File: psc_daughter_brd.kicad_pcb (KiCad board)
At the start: 2 copper layers, 50 x 150 mm, 293 parts, among them J1 61082-061400LF, J2 61082-061400LF, U1 AD8221, U10 BUF634AxD, U11 BUF634AxD, U12 ADR1001AEZ, U13 ADS8568SPM, U14 AD8221, U15 OPA277, U16 AD8221, U17 OPA277, U18 AD8221, U19 OPA277, U2 OPA277, U26 LTC6655BHLS8-5, U27 AD8429BRZ, U28 AD8675ARZ, U29 LT6202CS5, U3 AD8676xR, U30 LTC6363xMS8, U31 LTC2376CDE-20-PBF, U32 LTC6655BHLS8-5, U33 AD8429BRZ, U34 AD8675ARZ, U35 LT6202CS5, U36 LTC6363xMS8, U37 LTC2376CDE-20-PBF, U38 TXUN0104RUTR, U39 ADUM5240ARZ, U4 AD8676xR, U40 ADUM5240ARZ, U41 TXUN0104RUTR, U42 ADUM5242ARZ, U43 ADUM5242ARZ, U5 AD5791BRUZ, U6 AD797, U7 OPA277, U8 OPA277, U9 OPA277

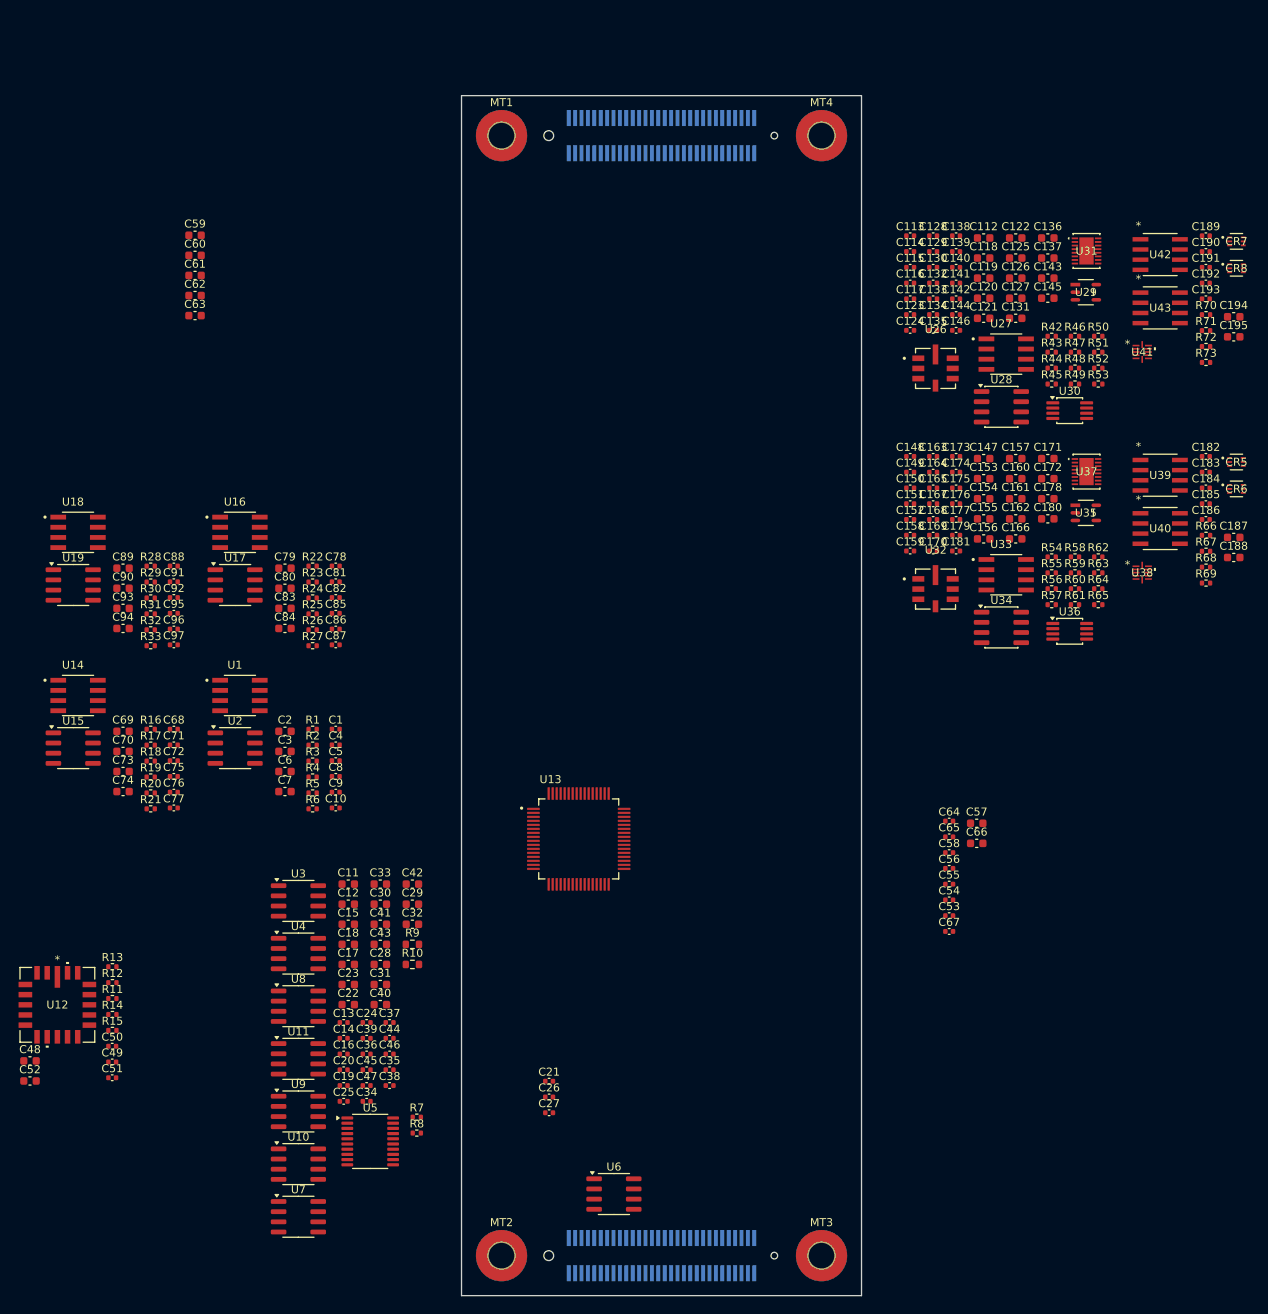
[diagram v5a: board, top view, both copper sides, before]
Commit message: DAC and DCCT placement
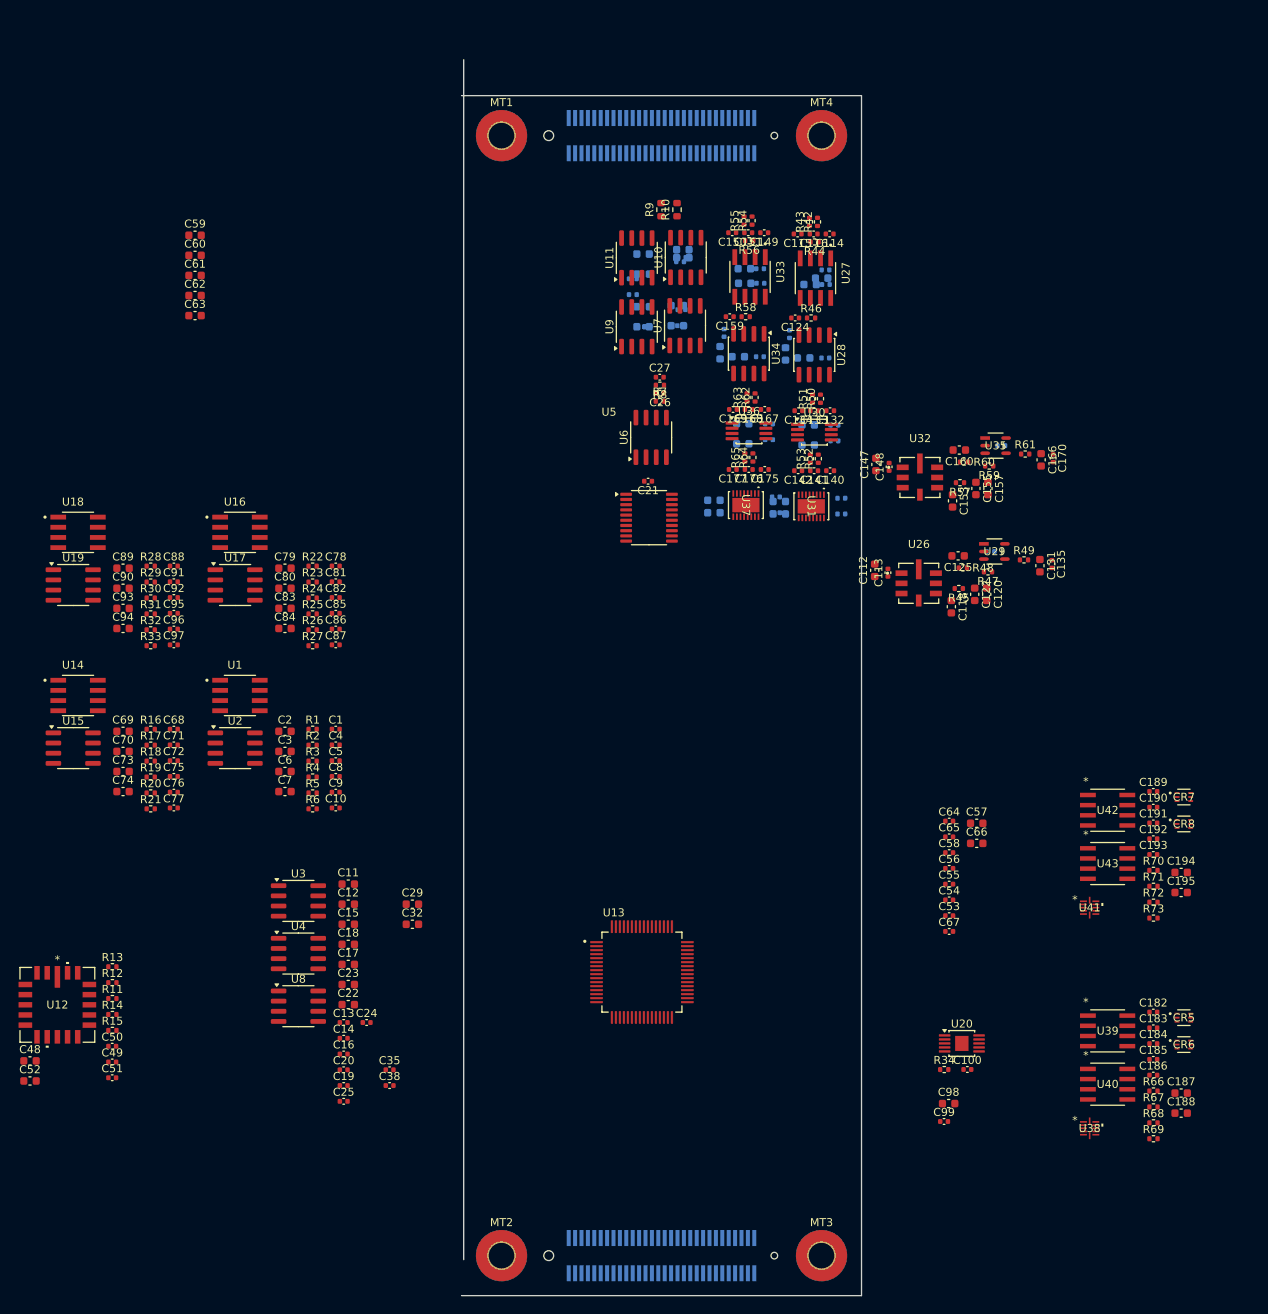
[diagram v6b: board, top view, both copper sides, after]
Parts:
- added C100: 0.47uF, Capacitor_SMD:C_0402_1005Metric, F.Cu at (202.9, 163.5)
- added C98: 10uF, Capacitor_SMD:C_0603_1608Metric, F.Cu at (200.6, 167.8)
- added C99: 0.1uF, Capacitor_SMD:C_0402_1005Metric, F.Cu at (200.0, 170.0)
- added R34: 121, Resistor_SMD:R_0402_1005Metric, F.Cu at (200.0, 163.5)
- added U20: LT3042xMSE, Package_SO:MSOP-10-1EP_3x3mm_P0.5mm_EP1.68x1.88mm, F.Cu at (202.2, 160.2)
- C117, C119, C121, C123, C126, C127, C128, C129, C130, C136, C137, C138, C139, C143, C144, C145, C146, C152, C154, C156, C158, C161, C162, C163, C164, C165, C171, C172, C173, C174, C178, C179, C180, C181, C28, C30, C31, C33, C34, C36, C37, C39, C40, C41, C42, C43, C44, C45, C46, C47: moved to B.Cu
- moved U10 123.2 mm to (167.7, 62.0), turned to 90 degrees
- moved U7 121.4 mm to (167.6, 70.5), turned to 90 degrees
- moved U11 108.7 mm to (161.6, 62.0), turned to 90 degrees
- moved U9 106.8 mm to (161.6, 70.7), turned to 90 degrees
- moved C46 105.5 mm to (167.0, 62.5), turned to 180 degrees
- moved C34 104.6 mm to (167.2, 70.5), turned to 180 degrees
- moved C45 104.3 mm to (161.1, 64.7), turned to 180 degrees
- moved C47 104.3 mm to (161.1, 66.6), turned to 180 degrees
- moved C44 104.2 mm to (167.3, 62.0), turned to 180 degrees
- moved C40 101.7 mm to (167.4, 61.0), turned to 180 degrees
- moved R10 100.0 mm to (166.6, 56.0), turned to 90 degrees
- moved R8 98.3 mm to (164.5, 78.0), turned to 180 degrees
- moved C36 97.1 mm to (162.1, 70.7), turned to 180 degrees
- moved R9 97.0 mm to (164.6, 56.0), turned to 90 degrees
- moved C37 96.3 mm to (167.2, 68.5), turned to 180 degrees
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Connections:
- net +10V renamed /DCCT ADCs/DCCT Channel 1/vref_in
- net /DCCT ADCs/dcct1_busy renamed /DCCT ADCs/DCCT Channel 2/busy
- C53 pad 1: Net-(C53-Pad1) -> +5.0V
- C54 pad 1: Net-(C53-Pad1) -> +5.0V
- C55 pad 1: Net-(C53-Pad1) -> +5.0V
- C56 pad 1: Net-(C53-Pad1) -> +5.0V
- C58 pad 1: Net-(C53-Pad1) -> +5.0V
- C65 pad 1: Net-(C53-Pad1) -> +5.0V
- J1 pad 1: unconnected-(J1-Pad1) -> /PS connector/dout_iso_gnd
- J1 pad 10: unconnected-(J1-Pad10) -> /PS connector/digin_acon
- J1 pad 11: unconnected-(J1-Pad11) -> /PS connector/din_iso_gnd
- J1 pad 12: /Isolated Digital IO/din0_iso -> /PS connector/digin_flt1
- J1 pad 13: unconnected-(J1-Pad13) -> /PS connector/din_iso_gnd
- J1 pad 14: /Isolated Digital IO/din1_iso -> /PS connector/digin_flt2
- J1 pad 15: unconnected-(J1-Pad15) -> /PS connector/din_iso_gnd
- J1 pad 16: /Isolated Digital IO/din2_iso -> /PS connector/digin_spare
- J1 pad 17: unconnected-(J1-Pad17) -> GND
- J1 pad 18: /Isolated Digital IO/din3_iso -> GND
- J1 pad 19: unconnected-(J1-Pad19) -> GND
- J1 pad 2: /Isolated Digital IO/dout0_iso -> /PS connector/digout_on1
- J1 pad 20: unconnected-(J1-Pad20) -> /Monitor ADCs/monitor_spare+
- J1 pad 21: unconnected-(J1-Pad21) -> GND
- J1 pad 22: unconnected-(J1-Pad22) -> /Monitor ADCs/monitor_spare-
- J1 pad 23: unconnected-(J1-Pad23) -> GND
- J1 pad 24: /Monitor ADCs/monitor_vout+ -> GND
- J1 pad 25: unconnected-(J1-Pad25) -> GND
- J1 pad 26: /Monitor ADCs/monitor_vout- -> /Monitor ADCs/monitor_ignd+
- J1 pad 27: unconnected-(J1-Pad27) -> GND
- J1 pad 28: unconnected-(J1-Pad28) -> /Monitor ADCs/monitor_ignd-
- J1 pad 29: unconnected-(J1-Pad29) -> GND
- J1 pad 3: unconnected-(J1-Pad3) -> /PS connector/dout_iso_gnd
- J1 pad 30: /Monitor ADCs/monitor_ignd+ -> GND
- J1 pad 31: unconnected-(J1-Pad31) -> GND
- J1 pad 32: /Monitor ADCs/monitor_ignd- -> /Monitor ADCs/monitor_vout+
- J1 pad 33: unconnected-(J1-Pad33) -> GND
- J1 pad 34: unconnected-(J1-Pad34) -> /Monitor ADCs/monitor_vout-
- J1 pad 35: unconnected-(J1-Pad35) -> +15V
- J1 pad 36: /Monitor ADCs/monitor_spare+ -> GND
- J1 pad 37: unconnected-(J1-Pad37) -> +15V
- J1 pad 38: /Monitor ADCs/monitor_spare- -> GND
- J1 pad 39: unconnected-(J1-Pad39) -> GND
- J1 pad 4: /Isolated Digital IO/dout1_iso -> /PS connector/digout_on2
- J1 pad 40: unconnected-(J1-Pad40) -> /DAC/dac_out+
- J1 pad 41: unconnected-(J1-Pad41) -> GND
- J1 pad 42: /DAC/dac_out+ -> /DAC/dac_vout-
- J1 pad 43: unconnected-(J1-Pad43) -> -15V
- J1 pad 44: /DAC/dac_vout- -> GND
- J1 pad 45: unconnected-(J1-Pad45) -> -15V
- J1 pad 46: unconnected-(J1-Pad46) -> GND
- J1 pad 47: unconnected-(J1-Pad47) -> GND
- J1 pad 48: unconnected-(J1-Pad48) -> /DCCT ADCs/dcct0+
- J1 pad 49: unconnected-(J1-Pad49) -> GND
- J1 pad 5: unconnected-(J1-Pad5) -> /PS connector/dout_iso_gnd
- J1 pad 50: /DCCT ADCs/dcct0+ -> /DCCT ADCs/dcct0-
- J1 pad 51: unconnected-(J1-Pad51) -> +5.3VA
- J1 pad 52: /DCCT ADCs/dcct0- -> -5.3VA
- J1 pad 53: unconnected-(J1-Pad53) -> +5.3VA
- J1 pad 54: unconnected-(J1-Pad54) -> -5.3VA
- J1 pad 55: unconnected-(J1-Pad55) -> GND
- J1 pad 57: unconnected-(J1-Pad57) -> GND
- J1 pad 59: unconnected-(J1-Pad59) -> GND
- J1 pad 6: /Isolated Digital IO/dout2_iso -> /PS connector/digout_reset
- J1 pad 60: unconnected-(J1-Pad60) -> GND
- J1 pad 7: unconnected-(J1-Pad7) -> /PS connector/dout_iso_gnd
- J1 pad 8: /Isolated Digital IO/dout3_iso -> /PS connector/digout_spare
- J1 pad 9: unconnected-(J1-Pad9) -> /PS connector/din_iso_gnd
- J2 pad 1: unconnected-(J2-Pad1) -> /FPGA connector/dout0
- J2 pad 10: unconnected-(J2-Pad10) -> +1.8V
- J2 pad 11: unconnected-(J2-Pad11) -> /FPGA connector/din1
- J2 pad 12: unconnected-(J2-Pad12) -> GND
- J2 pad 13: unconnected-(J2-Pad13) -> /FPGA connector/din2
- J2 pad 14: unconnected-(J2-Pad14) -> GND
- J2 pad 15: unconnected-(J2-Pad15) -> /FPGA connector/din3
- J2 pad 16: unconnected-(J2-Pad16) -> GND
- J2 pad 17: unconnected-(J2-Pad17) -> GND
- J2 pad 18: unconnected-(J2-Pad18) -> GND
- J2 pad 19: unconnected-(J2-Pad19) -> /DAC/sclk
- J2 pad 2: unconnected-(J2-Pad2) -> GND
- J2 pad 20: unconnected-(J2-Pad20) -> GND
- J2 pad 21: unconnected-(J2-Pad21) -> /DAC/sdin
- J2 pad 22: unconnected-(J2-Pad22) -> +3.3V
- J2 pad 23: unconnected-(J2-Pad23) -> /DAC/syncn
- J2 pad 24: unconnected-(J2-Pad24) -> +3.3V
- J2 pad 25: unconnected-(J2-Pad25) -> GND
- J2 pad 26: unconnected-(J2-Pad26) -> +3.3V
- J2 pad 27: unconnected-(J2-Pad27) -> /FPGA connector/mon_reset
- J2 pad 28: unconnected-(J2-Pad28) -> GND
- J2 pad 29: unconnected-(J2-Pad29) -> /FPGA connector/mon_convert
- J2 pad 3: unconnected-(J2-Pad3) -> /FPGA connector/dout1
- J2 pad 30: unconnected-(J2-Pad30) -> GND
- J2 pad 31: unconnected-(J2-Pad31) -> /FPGA connector/mon_busy
- J2 pad 32: unconnected-(J2-Pad32) -> GND
- J2 pad 33: unconnected-(J2-Pad33) -> /FPGA connector/mon_fs
- J2 pad 34: unconnected-(J2-Pad34) -> GND
- J2 pad 35: unconnected-(J2-Pad35) -> /FPGA connector/mon_sdo
- J2 pad 36: unconnected-(J2-Pad36) -> GND
- J2 pad 37: unconnected-(J2-Pad37) -> /FPGA connector/mon_sclk
- J2 pad 38: unconnected-(J2-Pad38) -> GND
- J2 pad 39: unconnected-(J2-Pad39) -> GND
- J2 pad 4: unconnected-(J2-Pad4) -> GND
- J2 pad 40: unconnected-(J2-Pad40) -> GND
- J2 pad 41: unconnected-(J2-Pad41) -> /DCCT ADCs/dcct_cnv
- J2 pad 42: unconnected-(J2-Pad42) -> +5.0V
- J2 pad 43: unconnected-(J2-Pad43) -> /DCCT ADCs/dcct_busy
- J2 pad 44: unconnected-(J2-Pad44) -> +5.0V
- J2 pad 45: unconnected-(J2-Pad45) -> /DCCT ADCs/dcct_sck
- J2 pad 46: unconnected-(J2-Pad46) -> +5.0V
- J2 pad 47: unconnected-(J2-Pad47) -> /DCCT ADCs/dcct0_sdo
- J2 pad 48: unconnected-(J2-Pad48) -> GND
- J2 pad 49: unconnected-(J2-Pad49) -> /DCCT ADCs/dcct1_sdo
- J2 pad 5: unconnected-(J2-Pad5) -> /FPGA connector/dout2
- J2 pad 50: unconnected-(J2-Pad50) -> GND
- J2 pad 51: unconnected-(J2-Pad51) -> GND
- J2 pad 52: unconnected-(J2-Pad52) -> GND
- J2 pad 53: unconnected-(J2-Pad53) -> GND
- J2 pad 54: unconnected-(J2-Pad54) -> GND
- J2 pad 55: unconnected-(J2-Pad55) -> GND
- J2 pad 56: unconnected-(J2-Pad56) -> GND
- J2 pad 57: unconnected-(J2-Pad57) -> GND
- J2 pad 58: unconnected-(J2-Pad58) -> GND
- J2 pad 59: unconnected-(J2-Pad59) -> GND
- J2 pad 6: unconnected-(J2-Pad6) -> +1.8V
- J2 pad 60: unconnected-(J2-Pad60) -> GND
- J2 pad 7: unconnected-(J2-Pad7) -> /FPGA connector/dout3
- J2 pad 8: unconnected-(J2-Pad8) -> +1.8V
- J2 pad 9: unconnected-(J2-Pad9) -> /FPGA connector/din0
- U13 pad 1: unconnected-(U13-HVSS-Pad1) -> -15V
- U13 pad 10: /Monitor ADCs/reset -> /FPGA connector/mon_reset
- U13 pad 13: /Monitor ADCs/fs -> /FPGA connector/mon_fs
- U13 pad 14: Net-(C53-Pad1) -> +5.0V
- U13 pad 19: /Monitor ADCs/sdo -> /FPGA connector/mon_sdo
- U13 pad 21: /Monitor ADCs/sclk -> /FPGA connector/mon_sclk
- U13 pad 35: /Monitor ADCs/busy -> /FPGA connector/mon_busy
- U13 pad 37: /Monitor ADCs/convert -> /FPGA connector/mon_convert
- U13 pad 38: /Monitor ADCs/convert -> /FPGA connector/mon_convert
- U13 pad 39: /Monitor ADCs/convert -> /FPGA connector/mon_convert
- U13 pad 4: Net-(C53-Pad1) -> +5.0V
- U13 pad 40: /Monitor ADCs/convert -> /FPGA connector/mon_convert
- U13 pad 45: Net-(C53-Pad1) -> +5.0V
- U13 pad 52: Net-(C53-Pad1) -> +5.0V
- U13 pad 57: Net-(C53-Pad1) -> +5.0V
- U13 pad 61: Net-(C53-Pad1) -> +5.0V
- U31 pad 13: /DCCT ADCs/dcct1_sck -> /DCCT ADCs/dcct_sck
- U31 pad 9: /DCCT ADCs/dcct1_cnv -> /DCCT ADCs/dcct_cnv
- U37 pad 11: /DCCT ADCs/dcct0_busy -> /DCCT ADCs/dcct_busy
- U37 pad 13: /DCCT ADCs/dcct0_sck -> /DCCT ADCs/dcct_sck
- U37 pad 9: /DCCT ADCs/dcct0_cnv -> /DCCT ADCs/dcct_cnv
- U38 pad 2: /Isolated Digital IO/dout0 -> /FPGA connector/dout0
- U38 pad 3: /Isolated Digital IO/dout1 -> /FPGA connector/dout1
- U38 pad 4: /Isolated Digital IO/dout2 -> /FPGA connector/dout2
- U38 pad 5: /Isolated Digital IO/dout3 -> /FPGA connector/dout3
- U41 pad 10: /Isolated Digital IO/din0 -> /FPGA connector/din0
- U41 pad 7: /Isolated Digital IO/din3 -> /FPGA connector/din3
- U41 pad 8: /Isolated Digital IO/din2 -> /FPGA connector/din2
- U41 pad 9: /Isolated Digital IO/din1 -> /FPGA connector/din1
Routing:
- added copper zone on In1.Cu, net GND
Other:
- board size 50 x 150 mm -> 50 x 154.5 mm
- copper layers 2 -> 10

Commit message: finish rough placement
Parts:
- removed C112, C118, C120, C122, C125, C131, C29, C32: 10uF, Capacitor_SMD:C_0603_1608Metric
- removed C113, C129, C135, C35, C38: 0.1uF, Capacitor_SMD:C_0402_1005Metric
- removed R45: 0, Resistor_SMD:R_0402_1005Metric
- removed R47, R48: 10K, Resistor_SMD:R_0402_1005Metric
- removed R49: 10, Resistor_SMD:R_0402_1005Metric
- removed U26: LTC6655BHLS8-5, myparts:LTC6655
- removed U29: LT6202CS5, myparts:LT6202CS5
- removed U4: AD8676xR, Package_SO:SOIC-8_3.9x4.9mm_P1.27mm
- removed U8: OPA277, Package_SO:SOIC-8_3.9x4.9mm_P1.27mm
- C10, C11, C12, C13, C14, C15, C16, C17, C18, C182, C183, C184, C185, C186, C187, C188, C189, C19, C190, C191, C192, C193, C194, C195, C2, C20, C22, C23, C24, C25, C3, C4, C48, C49, C5, C53, C54, C55, C56, C58, C6, C65, C69, C7, C70, C71, C72, C73, C74, C76, C77, C79, C80, C81, C82, C83, C84, C86, C87, C89, C9, C90, C91, C92, C93, C94, C96, C97: moved to B.Cu
- moved C59 121.7 mm to (176.4, 158.8)
- moved C60 110.5 mm to (170.8, 151.5), turned to 90 degrees
- moved C62 106.2 mm to (158.6, 159.2), turned to 180 degrees
- moved C61 104.7 mm to (164.2, 151.5), turned to 90 degrees
- moved C52 103.5 mm to (169.0, 103.5), turned to 180 degrees
- moved C63 102.6 mm to (167.8, 151.5), turned to 90 degrees
- moved C48 100.8 mm to (171.5, 109.5)
- moved C51 94.6 mm to (169.5, 105.0), turned to 180 degrees
- moved C50 93.7 mm to (171.5, 105.0)
- moved U12 93.5 mm to (171.5, 111.0), turned to 180 degrees
- moved C25 93.4 mm to (168.5, 84.8), turned to 180 degrees
- moved C19 92.6 mm to (177.5, 89.2)
- moved R14 91.5 mm to (177.5, 115.0), turned to -90 degrees
- moved C49 91.4 mm to (171.5, 111.0)
- moved C195 88.5 mm to (144.1, 164.0)
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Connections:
- net /DCCT ADCs/DCCT Channel 1/vref_in renamed Net-(U20-OUT)
- C155 pad 1: Net-(U37-REF) -> /DCCT ADCs/DCCT Channel 1/adc_vref
- C157 pad 1: Net-(U37-REF) -> /DCCT ADCs/DCCT Channel 1/adc_vref
- C166 pad 1: Net-(U36-VOCM) -> /DCCT ADCs/DCCT Channel 1/drv_vref
- C170 pad 1: Net-(U36-VOCM) -> /DCCT ADCs/DCCT Channel 1/drv_vref
- C182 pad 1: +1V8 -> +1.8V
- J1 pad 10: /PS connector/digin_acon -> /Isolated Digital IO/din0_iso
- J1 pad 12: /PS connector/digin_flt1 -> /Isolated Digital IO/din1_iso
- J1 pad 14: /PS connector/digin_flt2 -> /Isolated Digital IO/din2_iso
- J1 pad 16: /PS connector/digin_spare -> /Isolated Digital IO/din3_iso
- J1 pad 2: /PS connector/digout_on1 -> /Isolated Digital IO/dout0_iso
- J1 pad 4: /PS connector/digout_on2 -> /Isolated Digital IO/dout1_iso
- J1 pad 6: /PS connector/digout_reset -> /Isolated Digital IO/dout2_iso
- J1 pad 8: /PS connector/digout_spare -> /Isolated Digital IO/dout3_iso
- R57 pad 1: Net-(U37-REF) -> /DCCT ADCs/DCCT Channel 1/adc_vref
- R59 pad 2: Net-(U37-REF) -> /DCCT ADCs/DCCT Channel 1/adc_vref
- R61 pad 1: Net-(U36-VOCM) -> /DCCT ADCs/DCCT Channel 1/drv_vref
- U3 pad 5: (no net) -> GND
- U3 pad 6: (no net) -> Net-(U3B--)
- U3 pad 7: (no net) -> Net-(U5-V_{REFNF})
- U30 pad 2: Net-(U30-VOCM) -> /DCCT ADCs/DCCT Channel 1/drv_vref
- U31 pad 7: Net-(U31-REF) -> /DCCT ADCs/DCCT Channel 1/adc_vref
- U31 pad 8: Net-(U31-REF) -> /DCCT ADCs/DCCT Channel 1/adc_vref
- U36 pad 2: Net-(U36-VOCM) -> /DCCT ADCs/DCCT Channel 1/drv_vref
- U37 pad 7: Net-(U37-REF) -> /DCCT ADCs/DCCT Channel 1/adc_vref
- U37 pad 8: Net-(U37-REF) -> /DCCT ADCs/DCCT Channel 1/adc_vref
- U38 pad 1: +1V8 -> +1.8V
- U5 pad 17: Net-(U4A--) -> Net-(U3B--)
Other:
- board size 50 x 154.5 mm -> 40 x 160 mm

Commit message: Change DAC outputs to 1.8v
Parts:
- added C29: 0.1uF, Capacitor_SMD:C_0402_1005Metric, B.Cu at (171.3, 93.2)
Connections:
- J1 pad 27: GND -> +15V
- J1 pad 29: GND -> +15V
- J1 pad 43: -15V -> +5.3VA
- J1 pad 45: -15V -> +5.3VA
- J1 pad 51: +5.3VA -> -5.3VA
- J1 pad 52: -5.3VA -> GND
- J1 pad 53: +5.3VA -> -5.3VA
- J1 pad 54: -5.3VA -> GND
- U5 pad 10: +3.3V -> +1.8V
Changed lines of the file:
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@@
 			(layers "F.Cu" "F.Mask" "F.Paste")
 			(roundrect_rratio 0.25)
-			(net 6 "+3.3V")
+			(net 133 "+1.8V")
 			(pinfunction "IOV_{CC}")
 			(pintype "power_in")
@@
 		(fp_text user "*"
 			(at 0 -4.1148 180)
-			(unlocked yes)
 			(layer "F.Fab")
 			(effects
@@
 		(fp_text user "*"
 			(at 0 -4.1148 180)
+			(unlocked yes)
 			(layer "F.Fab")
 			(effects
@@
 			(size 0.5 2)
 			(layers "B.Cu" "B.Mask" "B.Paste")
-			(net 1 "GND")
+			(net 5 "+15V")
 			(pinfunction "27")
 			(pintype "passive")
@@
 			(size 0.5 2)
 			(layers "B.Cu" "B.Mask" "B.Paste")
-			(net 1 "GND")
+			(net 5 "+15V")
 			(pinfunction "29")
 			(pintype "passive")
@@
 			(size 0.5 2)
 			(layers "B.Cu" "B.Mask" "B.Paste")
-			(net 4 "-15V")
+			(net 130 "+5.3VA")
 			(pinfunction "43")
 			(pintype "passive")
@@
 			(size 0.5 2)
 			(layers "B.Cu" "B.Mask" "B.Paste")
-			(net 4 "-15V")
+			(net 130 "+5.3VA")
 			(pinfunction "45")
 			(pintype "passive")
@@
 			(size 0.5 2)
 			(layers "B.Cu" "B.Mask" "B.Paste")
-			(net 130 "+5.3VA")
+			(net 131 "-5.3VA")
 			(pinfunction "51")
 			(pintype "passive")
@@
 			(size 0.5 2)
 			(layers "B.Cu" "B.Mask" "B.Paste")
-			(net 131 "-5.3VA")
+			(net 1 "GND")
 			(pinfunction "52")
 			(pintype "passive")
@@
 			(size 0.5 2)
 			(layers "B.Cu" "B.Mask" "B.Paste")
-			(net 130 "+5.3VA")
+			(net 131 "-5.3VA")
 			(pinfunction "53")
 			(pintype "passive")
@@
 			(size 0.5 2)
 			(layers "B.Cu" "B.Mask" "B.Paste")
-			(net 131 "-5.3VA")
+			(net 1 "GND")
 			(pinfunction "54")
 			(pintype "passive")
@@
 			(size 0.56 0.62)
 			(layers "B.Cu" "B.Mask" "B.Paste")
+			(roundrect_rratio 0.25)
+			(net 1 "GND")
+			(pintype "passive")
+		)
+		(embedded_fonts no)
+		(model "${KICAD9_3DMODEL_DIR}/Capacitor_SMD.3dshapes/C_0402_1005Metric.step"
+			(offset
+				(xyz 0 0 0)
+			)
+			(scale
+				(xyz 1 1 1)
+			)
+			(rotate
+				(xyz 0 0 0)
+			)
+		)
+	)
+	(footprint "Capacitor_SMD:C_0402_1005Metric"
+		(layer "B.Cu")
+		(at 171.27 93.25)
+		(descr "Capacitor SMD 0402 (1005 Metric), square (rectangular) end terminal, IPC-7351 nominal, (Body size source: IPC-SM-782 page 76, https://www.pcb-3d.com/wordpress/wp-content/uploads/ipc-sm-782a_amendment_1_and_2.pdf), generated with kicad-footprint-generator")
+		(tags "capacitor")
+		(property "Reference" "C29"
+			(at 0 1.16 0)
+			(layer "B.SilkS")
+			(effects
+				(font
+					(size 1 1)
+					(thickness 0.15)
+				)
+				(justify mirror)
+			)
+		)
+		(property "Value" "0.1uF"
+			(at 0 -1.16 0)
+			(layer "B.Fab")
+			(effects
+				(font
+					(size 1 1)
+					(thickness 0.15)
+				)
+				(justify mirror)
+			)
+		)
+		(property "Datasheet" "~"
+			(at 0 0 0)
+			(layer "B.Fab")
+			(hide yes)
+			(effects
+				(font
+					(size 1.27 1.27)
+					(thickness 0.15)
+				)
+				(justify mirror)
+			)
+		)
+		(property "Description" "Unpolarized capacitor, small symbol"
+			(at 0 0 0)
+			(layer "B.Fab")
+			(hide yes)
+			(effects
+				(font
+					(size 1.27 1.27)
+					(thickness 0.15)
+				)
+				(justify mirror)
+			)
+		)
+		(property "Type" ""
+			(at 0 0 180)
+			(unlocked yes)
+			(layer "B.Fab")
+			(hide yes)
+			(effects
+				(font
+					(size 1 1)
+					(thickness 0.15)
+				)
+				(justify mirror)
+			)
+		)
+		(property ki_fp_filters "C_*")
+		(sheetname "/DAC/")
+		(sheetfile "dac.kicad_sch")
+		(attr smd)
+		(fp_line
+			(start -0.107836 -0.36)
+			(end 0.107836 -0.36)
+			(stroke
+				(width 0.12)
+				(type solid)
+			)
+			(layer "B.SilkS")
+		)
+		(fp_line
+			(start -0.107836 0.36)
+			(end 0.107836 0.36)
+			(stroke
+				(width 0.12)
+				(type solid)
+			)
+			(layer "B.SilkS")
+		)
+		(fp_line
+			(start -0.91 -0.46)
+			(end -0.91 0.46)
+			(stroke
+				(width 0.05)
+				(type solid)
+			)
+			(layer "B.CrtYd")
+		)
+		(fp_line
+			(start -0.91 0.46)
+			(end 0.91 0.46)
+			(stroke
+				(width 0.05)
+				(type solid)
+			)
+			(layer "B.CrtYd")
+		)
+		(fp_line
+			(start 0.91 -0.46)
+			(end -0.91 -0.46)
+			(stroke
+				(width 0.05)
+				(type solid)
+			)
+			(layer "B.CrtYd")
+		)
+		(fp_line
+			(start 0.91 0.46)
+			(end 0.91 -0.46)
+			(stroke
+				(width 0.05)
+				(type solid)
+			)
+			(layer "B.CrtYd")
+		)
+		(fp_line
+			(start -0.5 -0.25)
+			(end -0.5 0.25)
+			(stroke
+				(width 0.1)
+				(type solid)
+			)
+			(layer "B.Fab")
+		)
+		(fp_line
+			(start -0.5 0.25)
+			(end 0.5 0.25)
+			(stroke
+				(width 0.1)
+				(type solid)
+			)
+			(layer "B.Fab")
+		)
+		(fp_line
+			(start 0.5 -0.25)
+			(end -0.5 -0.25)
+			(stroke
+				(width 0.1)
+				(type solid)
+			)
+			(layer "B.Fab")
+		)
+		(fp_line
+			(start 0.5 0.25)
+			(end 0.5 -0.25)
+			(stroke
+				(width 0.1)
+				(type solid)
+			)
+			(layer "B.Fab")
+		)
+		(fp_text user "${REFERENCE}"
+			(at 0 0 0)
+			(layer "B.Fab")
+			(effects
+				(font
+					(size 0.25 0.25)
+					(thickness 0.04)
+				)
+				(justify mirror)
+			)
+		)
+		(pad "1" smd roundrect
+			(at -0.48 0)
+			(size 0.56 0.62)
+			(layers "B.Cu" "B.Mask" "B.Paste")
+			(roundrect_rratio 0.25)
+			(net 133 "+1.8V")
+			(pintype "passive")
+		)
+		(pad "2" smd roundrect
+			(at 0.48 0)
+			(size 0.56 0.62)
+			(layers "B.Cu" "B.Mask" "B.Paste")
